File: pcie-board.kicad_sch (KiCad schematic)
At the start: 0 parts

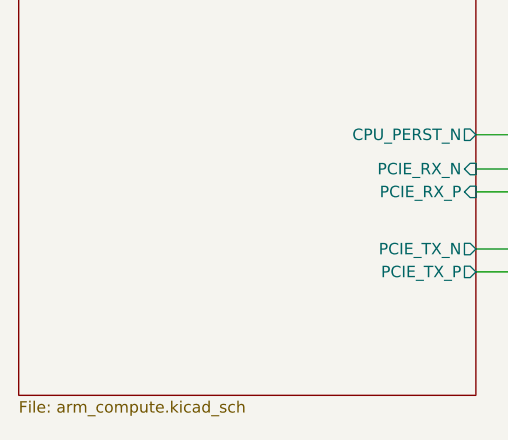
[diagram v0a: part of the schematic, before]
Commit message: add CPU_REFCLK_IN
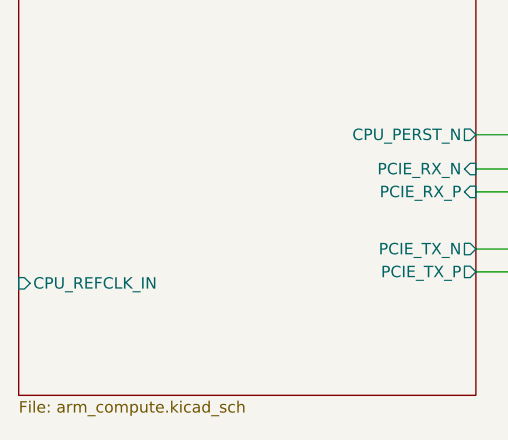
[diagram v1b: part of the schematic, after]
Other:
- sheet ARM Compute ports: added CPU_REFCLK_IN; removed none
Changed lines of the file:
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@@
+			)
+		)
+		(pin "CPU_REFCLK_IN" input
+			(at 50.546 63.5 180)
+			(effects
+				(font
+					(size 1.27 1.27)
+				)
+				(justify left)
 			)
 		)
